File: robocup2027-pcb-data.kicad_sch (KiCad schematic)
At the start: 7 parts, among them U1 ESP32-DEVKITC-32E

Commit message: new data
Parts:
- added C2: 1000uF, symbol Device:C_Polarized
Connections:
- net +6V: now also C2.1
- net GND: now also U1.J3_1 (GND_J3_1), C2.2
- net LiPo+: now reaches S1.1, U3.1 (+), U4.1 (Vin)
- net I2C_SCL: now reaches U1.J3_3 (IO22)
- net I2C_SDA: now reaches U1.J3_6 (IO21)
- no-connect marks 2 -> 4
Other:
- note added: "Buck-Boost converter"
- note added: "Voltmeter for 6V"
- note added: "batteries"
- moved on the sheet: U4

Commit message: updating schematics
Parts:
- added C1, C3, C4, C5, C6, C7: 0.1uF, symbol Device:C
- added M1, M2, M3, M4: ~, symbol robo:STS3032
- added R1, R2: 8.4k, symbol Device:R
- added U10, U5, U6, U7, U8, U9: ~, symbol robo:Tof-VL53L0X
- added U11: ~, symbol robo:DCDC-3.3v
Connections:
- net +6V: now also M1.2 (VCC), M2.2 (VCC), M3.2 (VCC), M4.2 (VCC)
- net GND: now also C1.2, C3.2, C4.2, C5.2, C6.2, C7.2, M1.1 (GND), M2.1 (GND), M3.1 (GND), M4.1 (GND), U10.2 (GND), U11.2 (GND), U5.2 (GND), U6.2 (GND), U7.2 (GND), U8.2 (GND), U9.2 (GND)
- net I2C_SCL: now also R1.2, U10.4 (SCL), U5.4 (SCL), U6.4 (SCL), U7.4 (SCL), U8.4 (SCL), U9.4 (SCL)
- net I2C_SDA: now also R2.2, U10.3 (SDA), U5.3 (SDA), U6.3 (SDA), U7.3 (SDA), U8.3 (SDA), U9.3 (SDA)
- net LiPo+: now also U11.1 (+Vin)
- new net +3.3V: C1.1, C3.1, C4.1, C5.1, C6.1, C7.1, R1.1, R2.1, U10.1 (V+), U11.3 (+Vout), U5.1 (V+), U6.1 (V+), U7.1 (V+), U8.1 (V+), U9.1 (V+)
- new net MOTOR_1: M1.3 (Signal)
- new net MOTOR_2: M2.3 (Signal)
- new net MOTOR_3: M3.3 (Signal)
- new net MOTOR_4: M4.3 (Signal)
- no-connect marks 4 -> 47
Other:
- note added: "3.3V buck converter"
- note added: "motors"
- moved on the sheet: C2, F1, L1, S1, U1, U2, U3, U4

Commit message: end of the day
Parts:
- added M5, M6: Motor_Servo, symbol Motor:Motor_Servo
- added Q1, Q2: BPW40, LED_THT:LED_D5.0mm_Clear, symbol Sensor_Optical:BPW40
- added R3: 100k, symbol Device:R
- added R4, R5: R, symbol Device:R
- added S2: tactile switch, 4-1437565-0:SW_4-1437565-0, symbol robo:tactile switch
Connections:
- net +3.3V: now also Q1.1 (C), Q2.1 (C)
- net GND: now also M5.3 (-), M6.3 (-), R3.2, R4.2, R5.2
- net at U1.J2_1 (3V3): now also S2.1
- net +5V: now reaches U1.J2_19 (EXT_5V)
- net +5V: now also M5.2 (+), M6.2 (+)
- net SG90_1_SIG: now reaches U1.J2_7 (IO32)
- net SG90_1_SIG: now also M5.1 (PWM)
- net at U1.J2_9 (IO25): now also R3.1, S2.2
- new net SG90_2_SIG: M6.1 (PWM)
- new net photoresistor_1: Q1.2 (E), R4.1
- new net photoresistor_2: Q2.2 (E), R5.1
- no-connect marks 47 -> 43
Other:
- note added: "ToF sensors"
- note added: "not assigned"
- moved on the sheet: C1, C3, C4, C5, C6, C7, R1, R2, U1, U10, U11, U5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

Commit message: end of the day
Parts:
- added D1, D2: 1N4001, Diode_THT:D_DO-41_SOD81_P10.16mm_Horizontal, symbol Diode:1N4001
- added U12, U13: ~, symbol robo:AE-HX711-SIP
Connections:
- net +3.3V: now also S2.1, D1.1 (K), D2.1 (K), U12.5 (VDD), U13.5 (VDD); no longer U11.3 (+Vout)
- net GND: now also U12.10 (GND), U13.10 (GND)
- net at U1.J2_1 (3V3): now also D1.2 (A); no longer S2.1
- new net: D2.2 (A), U11.3 (+Vout)
- new net load1_CLK: U12.7 (CLK)
- new net load1_DAT: U12.6 (DAT)
- new net load2_CLK: U13.7 (CLK)
- new net load2_DAT: U13.6 (DAT)
- no-connect marks 43 -> 55
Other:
- moved on the sheet: Q1, Q2, R4, R5

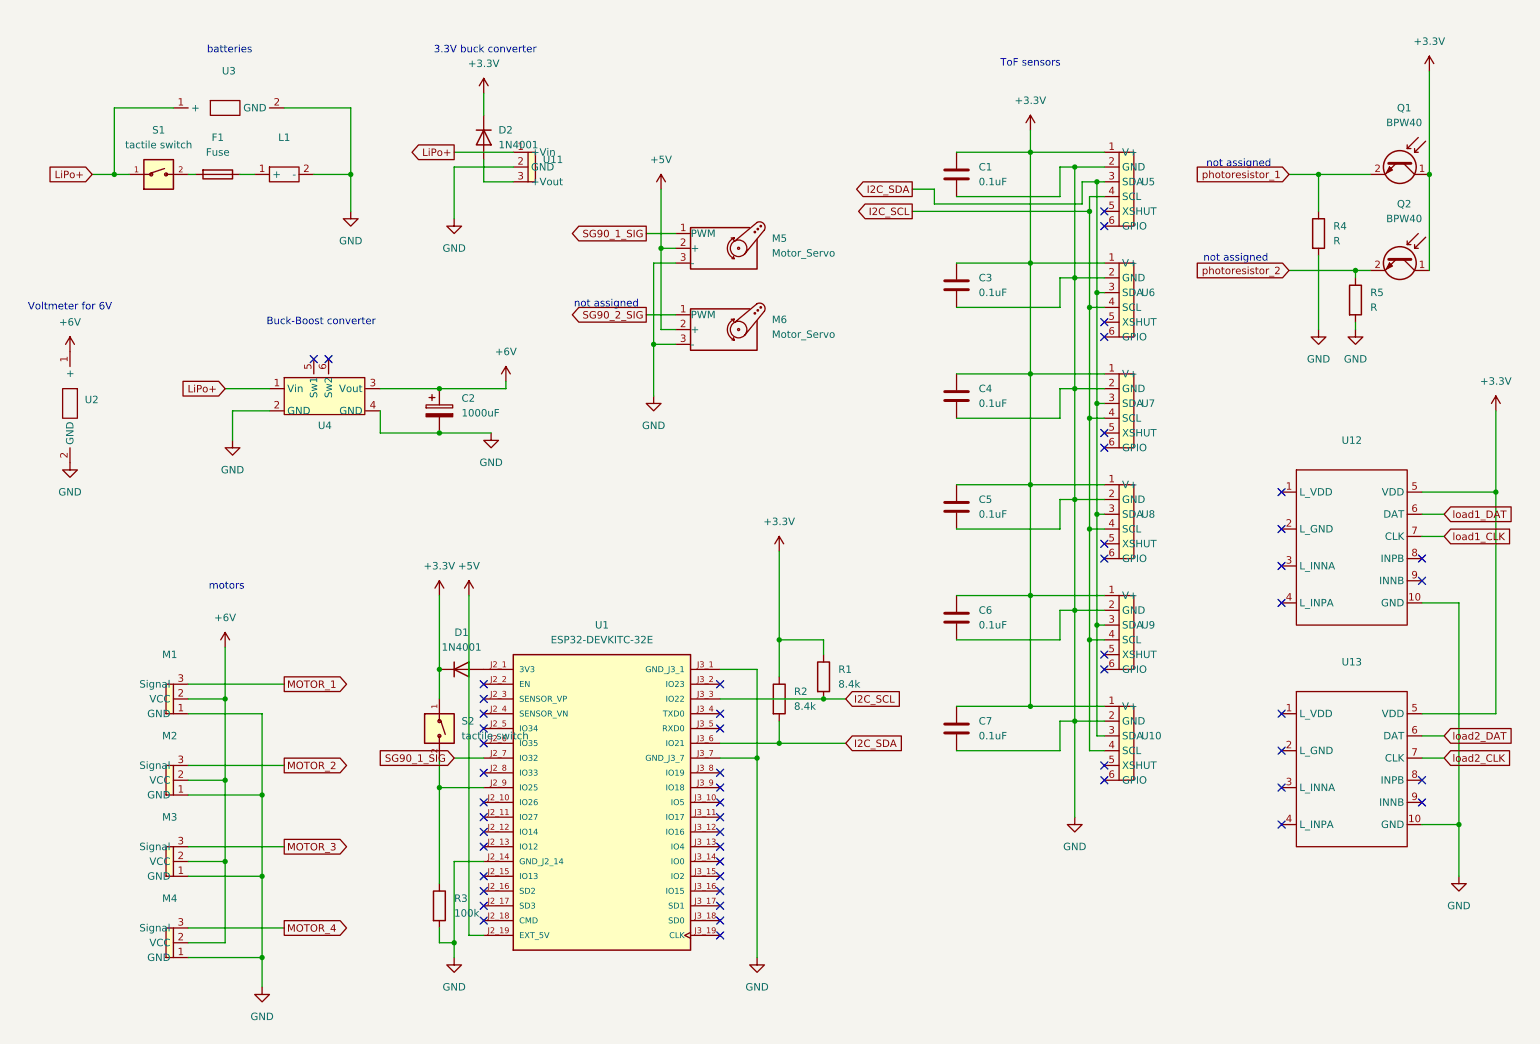
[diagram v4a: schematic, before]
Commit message: done with schematics
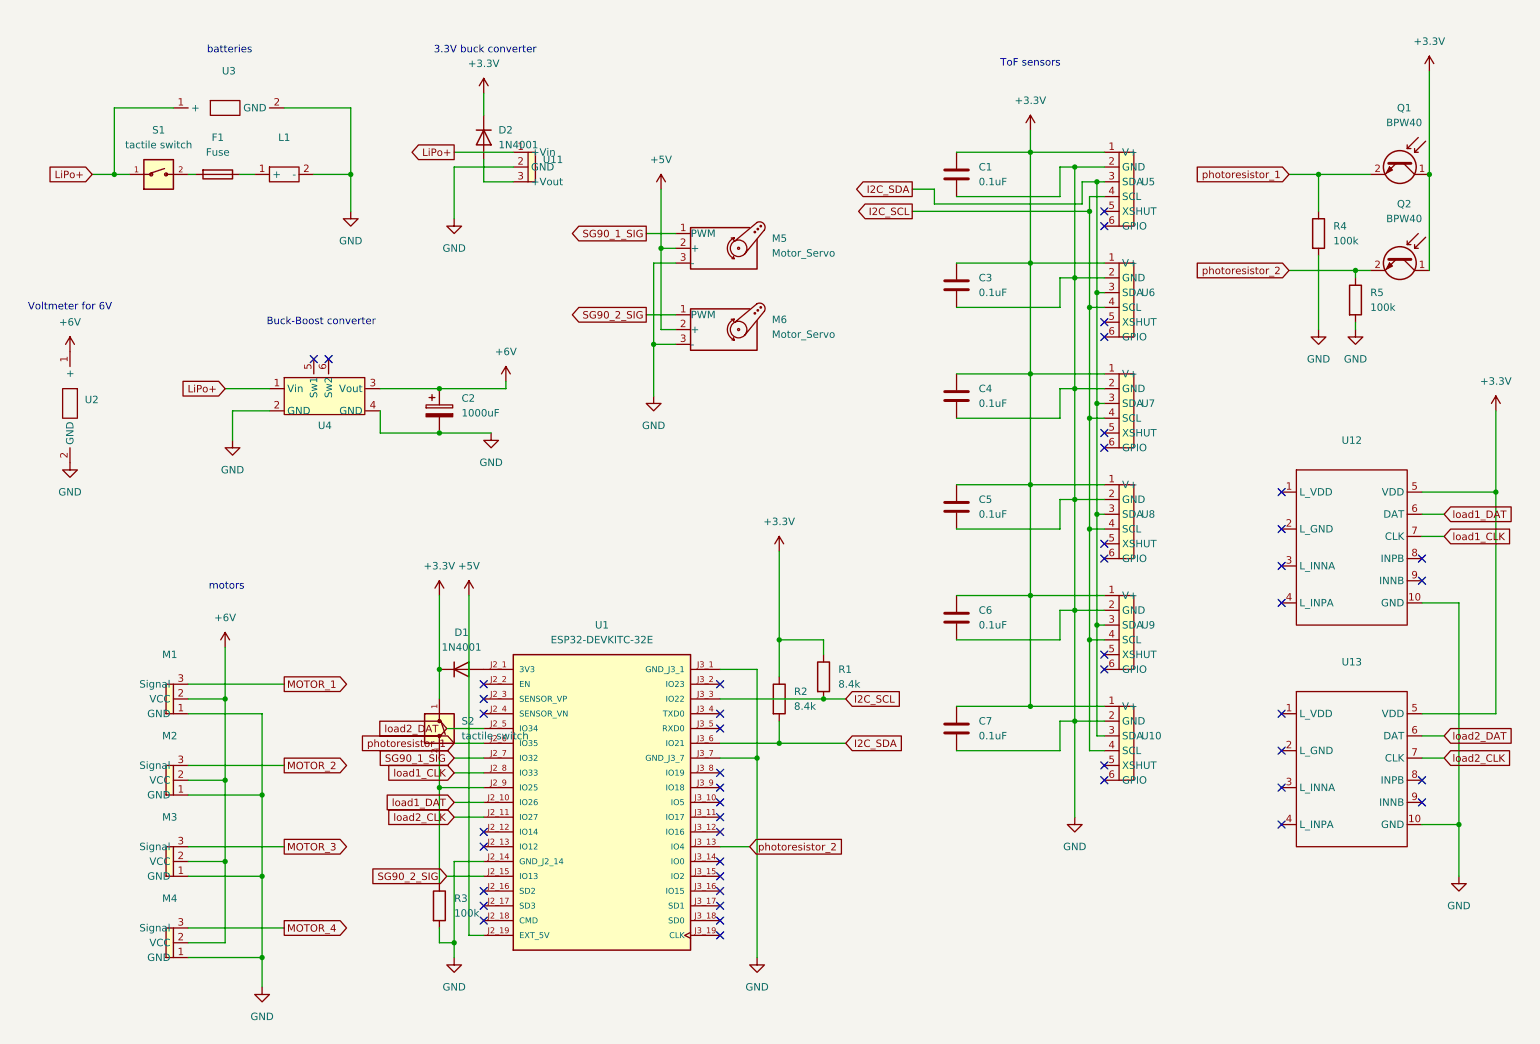
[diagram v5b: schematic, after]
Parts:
- R4, R5: value R -> 100k
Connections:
- net SG90_2_SIG: now also U1.J2_15 (IO13)
- net load1_CLK: now also U1.J2_8 (IO33)
- net load1_DAT: now also U1.J2_10 (IO26)
- net load2_CLK: now also U1.J2_11 (IO27)
- net load2_DAT: now also U1.J2_5 (IO34)
- net photoresistor_1: now also U1.J2_6 (IO35)
- net photoresistor_2: now also U1.J3_13 (IO4)
- no-connect marks 55 -> 48
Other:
- note removed: "not assigned"
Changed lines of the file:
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@@
 	(generator_version "9.0")
 	(paper "A3")
-	(text "not assigned"
-		(exclude_from_sim no)
-		(at 115.062 60.452 0)
-		(effects
-			(font
-				(size 1.27 1.27)
-			)
-		)
-	)
 	(text "batteries"
 		(exclude_from_sim no)
@@
 		)
 	)
-	(text "not assigned"
-		(exclude_from_sim no)
-		(at 223.266 52.578 0)
-		(effects
-			(font
-				(size 1.27 1.27)
-			)
-		)
-	)
-	(text "not assigned"
-		(exclude_from_sim no)
-		(at 223.774 36.322 0)
-		(effects
-			(font
-				(size 1.27 1.27)
-			)
-		)
-	)
 	(text "Voltmeter for 6V\n"
 		(exclude_from_sim no)
@@
 	)
 	(no_connect
-		(at 93.98 133.35)
-	)
-	(no_connect
 		(at 134.62 161.29)
 	)
@@
 	)
 	(no_connect
-		(at 93.98 146.05)
-	)
-	(no_connect
 		(at 200.66 104.14)
 	)
@@
 	)
 	(no_connect
-		(at 93.98 135.89)
-	)
-	(no_connect
 		(at 231.14 105.41)
 	)
@@
 	)
 	(no_connect
-		(at 93.98 140.97)
-	)
-	(no_connect
 		(at 134.62 166.37)
 	)
@@
 	)
 	(no_connect
-		(at 93.98 148.59)
-	)
-	(no_connect
 		(at 134.62 168.91)
 	)
@@
 	)
 	(no_connect
-		(at 134.62 153.67)
-	)
-	(no_connect
 		(at 200.66 123.19)
 	)
@@
 	)
 	(no_connect
-		(at 93.98 158.75)
-	)
-	(no_connect
 		(at 93.98 125.73)
 	)
@@
 	(wire
 		(pts
+			(xy 88.9 135.89) (xy 93.98 135.89)
+		)
+		(stroke
+			(width 0)
+			(type default)
+		)
+	)
+	(wire
+		(pts
 			(xy 71.12 26.67) (xy 71.12 38.1)
 		)
@@
 	(wire
 		(pts
+			(xy 87.63 133.35) (xy 93.98 133.35)
+		)
+		(stroke
+			(width 0)
+			(type default)
+		)
+	)
+	(wire
+		(pts
 			(xy 200.66 72.39) (xy 187.96 72.39)
 		)
@@
 	(wire
 		(pts
+			(xy 88.9 140.97) (xy 93.98 140.97)
+		)
+		(stroke
+			(width 0)
+			(type default)
+		)
+	)
+	(wire
+		(pts
 			(xy 175.26 53.34) (xy 187.96 53.34)
 		)
@@
 	(wire
 		(pts
+			(xy 87.63 158.75) (xy 93.98 158.75)
+		)
+		(stroke
+			(width 0)
+			(type default)
+		)
+	)
+	(wire
+		(pts
 			(xy 246.38 54.61) (xy 243.84 54.61)
 		)
@@
 	(wire
 		(pts
+			(xy 88.9 146.05) (xy 93.98 146.05)
+		)
+		(stroke
+			(width 0)
+			(type default)
+		)
+	)
+	(wire
+		(pts
 			(xy 88.9 36.83) (xy 88.9 45.72)
 		)
@@
 	(wire
 		(pts
+			(xy 88.9 148.59) (xy 93.98 148.59)
+		)
+		(stroke
+			(width 0)
+			(type default)
+		)
+	)
+	(wire
+		(pts
 			(xy 198.12 80.01) (xy 198.12 99.06)
 		)
@@
 	(wire
 		(pts
+			(xy 134.62 153.67) (xy 139.7 153.67)
+		)
+		(stroke
+			(width 0)
+			(type default)
+		)
+	)
+	(wire
+		(pts
 			(xy 152.4 118.11) (xy 152.4 120.65)
 		)
@@
 		)
 	)
+	(global_label "SG90_2_SIG"
+		(shape input)
+		(at 87.63 158.75 180)
+		(fields_autoplaced yes)
+		(effects
+			(font
+				(size 1.27 1.27)
+			)
+			(justify right)
+		)
+		(property "Intersheetrefs" "${INTERSHEET_REFS}"
+			(at 73.5173 158.75 0)
+			(effects
+				(font
+					(size 1.27 1.27)
+				)
+				(justify right)
+				(hide yes)
+			)
+		)
+	)
 	(global_label "MOTOR_1"
 		(shape output)
@@
 		)
 	)
+	(global_label "load2_DAT"
+		(shape input)
+		(at 87.63 133.35 180)
+		(fields_autoplaced yes)
+		(effects
+			(font
+				(size 1.27 1.27)
+			)
+			(justify right)
+		)
+		(property "Intersheetrefs" "${INTERSHEET_REFS}"
+			(at 75.0293 133.35 0)
+			(effects
+				(font
+					(size 1.27 1.27)
+				)
+				(justify right)
+				(hide yes)
+			)
+		)
+	)
+	(global_label "load1_DAT"
+		(shape input)
+		(at 88.9 146.05 180)
+		(fields_autoplaced yes)
+		(effects
+			(font
+				(size 1.27 1.27)
+			)
+			(justify right)
+		)
+		(property "Intersheetrefs" "${INTERSHEET_REFS}"
+			(at 76.2993 146.05 0)
+			(effects
+				(font
+					(size 1.27 1.27)
+				)
+				(justify right)
+				(hide yes)
+			)
+		)
+	)
 	(global_label "MOTOR_4"
 		(shape output)
@@
 		)
 	)
+	(global_label "load2_CLK"
+		(shape input)
+		(at 88.9 148.59 180)
+		(fields_autoplaced yes)
+		(effects
+			(font
+				(size 1.27 1.27)
+			)
+			(justify right)
+		)
+		(property "Intersheetrefs" "${INTERSHEET_REFS}"
+			(at 76.0574 148.59 0)
+			(effects
+				(font
+					(size 1.27 1.27)
+				)
+				(justify right)
+				(hide yes)
+			)
+		)
+	)
+	(global_label "photoresistor_2"
+		(shape input)
+		(at 139.7 153.67 0)
+		(fields_autoplaced yes)
+		(effects
+			(font
+				(size 1.27 1.27)
+			)
+			(justify left)
+		)
+		(property "Intersheetrefs" "${INTERSHEET_REFS}"
+			(at 157.3807 153.67 0)
+			(effects
+				(font
+					(size 1.27 1.27)
+				)
+				(justify left)
+				(hide yes)
+			)
+		)
+	)
 	(global_label "LiPo+"
 		(shape output)
@@
 		)
 	)
+	(global_label "photoresistor_1"
+		(shape input)
+		(at 88.9 135.89 180)
+		(fields_autoplaced yes)
+		(effects
+			(font
+				(size 1.27 1.27)
+			)
+			(justify right)
+		)
+		(property "Intersheetrefs" "${INTERSHEET_REFS}"
+			(at 71.2193 135.89 0)
+			(effects
+				(font
+					(size 1.27 1.27)
+				)
+				(justify right)
+				(hide yes)
+			)
+		)
+	)
 	(global_label "I2C_SCL"
 		(shape output)
@@
 		)
 	)
+	(global_label "load1_CLK"
+		(shape input)
+		(at 88.9 140.97 180)
+		(fields_autoplaced yes)
+		(effects
+			(font
+				(size 1.27 1.27)
+			)
+			(justify right)
+		)
+		(property "Intersheetrefs" "${INTERSHEET_REFS}"
+			(at 76.0574 140.97 0)
+			(effects
+				(font
+					(size 1.27 1.27)
+				)
+				(justify right)
+				(hide yes)
+			)
+		)
+	)
 	(global_label "SG90_1_SIG"
 		(shape output)
@@
 			)
 		)
-		(property "Value" "R"
+		(property "Value" "100k"
 			(at 240.03 49.5299 0)
 			(effects
@@
 			)
 		)
-		(property "Value" "R"
+		(property "Value" "100k"
 			(at 246.38 60.9599 0)
 			(effects

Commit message: update stuff
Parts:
- removed U13: ~, symbol robo:AE-HX711-SIP
- removed U4: ~, symbol robo:DCDC-LTC3111
- added C8: 1000uF, symbol Device:C_Polarized
- added U14: ~, robo:DCDC-LTC3111, symbol robo:DCDC-LTC3111
- added U4: ~, symbol robo:AE-HX711-SIP
- S1, S2: footprint 4-1437565-0:SW_4-1437565-0 -> robo:DS-850K-S-ON
- U2: footprint (none) -> robo:DS-850K-S-ON
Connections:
- net +3.3V: now also C8.1, U4.5 (VDD)
- net +6V: now also U14.3 (Vout)
- net GND: now also C8.2, U14.2 (GND), U14.4 (GND), U4.10 (GND)
- net LiPo+: now also U14.1 (Vin)
- net load1_CLK: now also U4.7 (CLK); no longer U12.7 (CLK)
- net load1_DAT: now also U4.6 (DAT); no longer U12.6 (DAT)
- net load2_CLK: now also U12.7 (CLK)
- net load2_DAT: now also U12.6 (DAT)

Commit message: update library
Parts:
- C1, C3, C4, C5, C6, C7: footprint (none) -> robo:2.54mm_capacitor
- C2: footprint (none) -> robo:5.08mm_capacitor_1
- C8: value 1000uF -> 470uF; footprint (none) -> robo:5.08mm_capacitor_1
- L1: footprint (none) -> robo:LiPo
- M5, M6: footprint (none) -> robo:servo_motor_3
- U3: footprint (none) -> robo:voltmeter
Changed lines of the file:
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@@
 	(wire
 		(pts
-			(xy 87.63 133.35) (xy 93.98 133.35)
+			(xy 83.82 133.35) (xy 93.98 133.35)
 		)
 		(stroke
@@
 	(wire
 		(pts
-			(xy 88.9 34.29) (xy 99.06 34.29)
+			(xy 97.79 45.72) (xy 97.79 34.29)
 		)
 		(stroke
@@
 	(wire
 		(pts
+			(xy 97.79 34.29) (xy 99.06 34.29)
+		)
+		(stroke
+			(width 0)
+			(type default)
+		)
+	)
+	(wire
+		(pts
 			(xy 91.44 114.3) (xy 91.44 168.91)
 		)
@@
 	(global_label "load2_DAT"
 		(shape input)
-		(at 87.63 133.35 180)
+		(at 83.82 133.35 180)
 		(fields_autoplaced yes)
 		(effects
@@
 		)
 		(property "Intersheetrefs" "${INTERSHEET_REFS}"
-			(at 75.0293 133.35 0)
+			(at 71.2193 133.35 0)
 			(effects
 				(font
@@
 	(global_label "LiPo+"
 		(shape output)
-		(at 88.9 34.29 180)
+		(at 97.79 45.72 270)
 		(fields_autoplaced yes)
 		(effects
@@
 		)
 		(property "Intersheetrefs" "${INTERSHEET_REFS}"
-			(at 80.2905 34.29 0)
+			(at 97.79 54.3295 90)
 			(effects
 				(font
@@
 			)
 		)
-		(property "Footprint" ""
+		(property "Footprint" "robo:voltmeter"
 			(at 49.53 26.67 0)
 			(effects
@@
 			)
 		)
-		(property "Footprint" ""
+		(property "Footprint" "robo:5.08mm_capacitor_1"
 			(at 87.3252 82.55 0)
 			(effects
@@
 			)
 		)
-		(property "Footprint" ""
+		(property "Footprint" "robo:servo_motor_3"
 			(at 134.62 55.626 0)
 			(effects
@@
 			)
 		)
-		(property "Footprint" ""
+		(property "Footprint" "robo:2.54mm_capacitor"
 			(at 176.2252 118.11 0)
 			(effects
@@
 			)
 		)
-		(property "Footprint" ""
+		(property "Footprint" "robo:LiPo"
 			(at 59.69 38.1 0)
 			(effects
@@
 			)
 		)
-		(property "Footprint" ""
+		(property "Footprint" "robo:servo_motor_3"
 			(at 134.62 69.596 0)
 			(effects
@@
 			)
 		)
-		(property "Footprint" ""
+		(property "Footprint" "robo:2.54mm_capacitor"
 			(at 176.2252 41.91 0)
 			(effects
@@
 			)
 		)
-		(property "Footprint" ""
+		(property "Footprint" "robo:2.54mm_capacitor"
 			(at 176.2252 60.96 0)
 			(effects
@@
 		(on_board yes)
 		(dnp no)
-		(fields_autoplaced yes)
 		(property "Reference" "C8"
-			(at 95.25 30.8609 0)
+			(at 85.598 29.718 0)
 			(effects
 				(font
@@
 			)
 		)
-		(property "Value" "1000uF"
-			(at 95.25 33.4009 0)
+		(property "Value" "470uF"
+			(at 80.772 33.02 0)
 			(effects
 				(font
@@
 			)
 		)
-		(property "Footprint" ""
+		(property "Footprint" "robo:5.08mm_capacitor_1"
 			(at 92.4052 36.83 0)
 			(effects
@@
 			)
 		)
-		(property "Footprint" ""
+		(property "Footprint" "robo:2.54mm_capacitor"
 			(at 176.2252 80.01 0)
 			(effects
@@
 			)
 		)
-		(property "Footprint" ""
+		(property "Footprint" "robo:2.54mm_capacitor"
 			(at 176.2252 137.16 0)
 			(effects
@@
 			)
 		)
-		(property "Footprint" ""
+		(property "Footprint" "robo:2.54mm_capacitor"
 			(at 176.2252 99.06 0)
 			(effects
@@
 		(on_board yes)
 		(dnp no)
-		(fields_autoplaced yes)
 		(property "Reference" "D2"
-			(at 96.52 30.4799 90)
+			(at 98.806 29.972 90)
 			(effects
 				(font
@@
 		)
 		(property "Value" "1N4001"
-			(at 96.52 33.0199 90)
+			(at 96.012 28.448 90)
 			(effects
 				(font

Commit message: update
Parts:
- F1: footprint (none) -> robo:5.08mm_capacitor_1
- R1, R2, R3, R4, R5: footprint (none) -> robo:Resister
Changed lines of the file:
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@@
 			)
 		)
-		(property "Footprint" ""
+		(property "Footprint" "robo:Resister"
 			(at 235.712 48.26 90)
 			(effects
@@
 			)
 		)
-		(property "Footprint" ""
+		(property "Footprint" "robo:Resister"
 			(at 143.002 128.27 90)
 			(effects
@@
 			)
 		)
-		(property "Footprint" ""
+		(property "Footprint" "robo:5.08mm_capacitor_1"
 			(at 48.26 36.322 90)
 			(effects
@@
 			)
 		)
-		(property "Footprint" ""
+		(property "Footprint" "robo:Resister"
 			(at 242.062 59.69 90)
 			(effects
@@
 			)
 		)
-		(property "Footprint" ""
+		(property "Footprint" "robo:Resister"
 			(at 84.582 163.83 90)
 			(effects
@@
 			)
 		)
-		(property "Footprint" ""
+		(property "Footprint" "robo:Resister"
 			(at 150.622 124.46 90)
 			(effects
